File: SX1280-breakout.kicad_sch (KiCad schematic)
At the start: 36 parts, among them J1 Conn_01x01, J10 Conn_01x01, J11 Conn_01x01, J12 Conn_01x01, J13 Conn_01x01, J14 Conn_01x01, J15 Conn_01x01, J16 Conn_01x01, J17 u.FL, J18 u.FL, J2 Conn_01x01, J3 Conn_01x01, J4 Conn_01x01, J5 Conn_01x01, J6 Conn_01x01, J7 Conn_01x01, J8 Conn_01x01, J9 Conn_01x01, U1 SX1280IMLTRT, U2 2450FM07D0034T, U3 EP2W+, X1 52.000 MHz

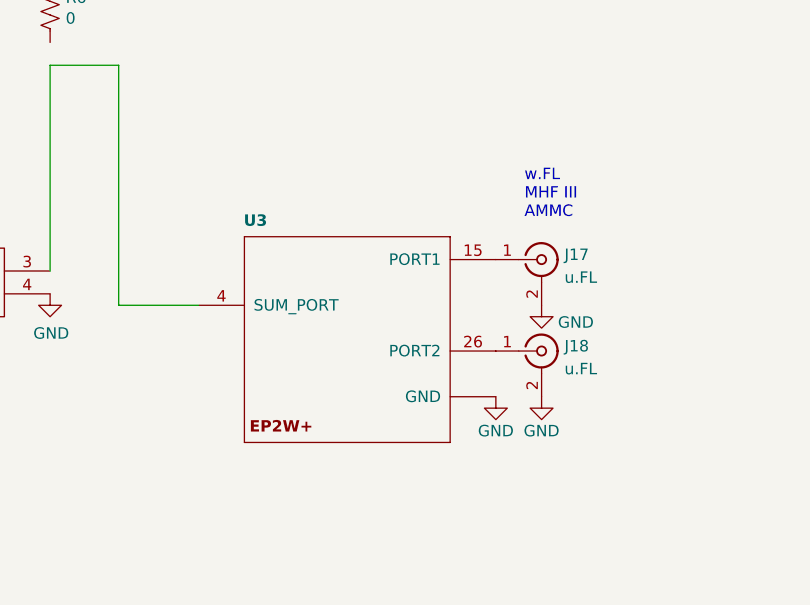
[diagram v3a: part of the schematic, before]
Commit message: back to single antenna
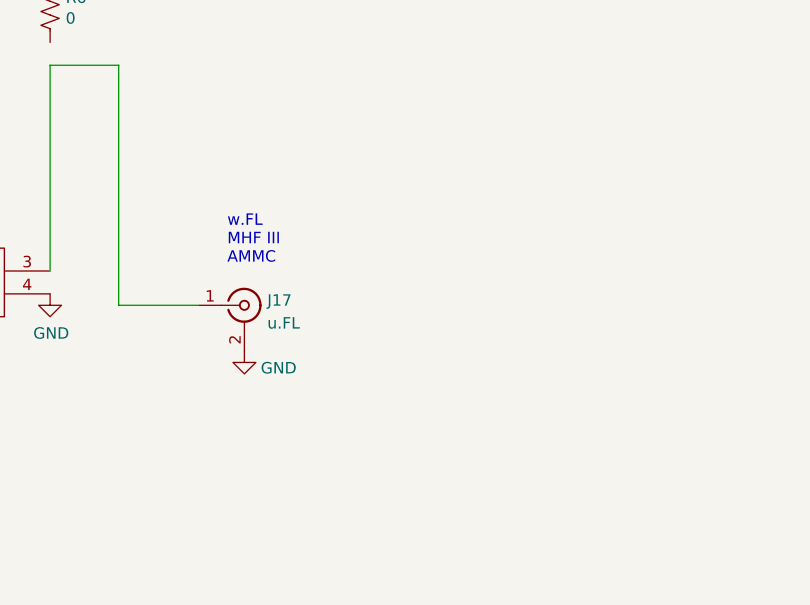
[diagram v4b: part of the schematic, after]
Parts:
- removed J18: u.FL, Connector_Coaxial:U.FL_Hirose_U.FL-R-SMT-1_Vertical, symbol Connector:Conn_Coaxial
- removed U3: EP2W+, custom-footprints:QFN32-5X5MM, symbol mainboard:EP2W+
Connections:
- net at U2.3 (OUT): now also J17.1 (In)
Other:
- moved on the sheet: J17
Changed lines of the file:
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@@
     (effects (font (size 3.9878 3.9878) (thickness 0.7976) bold) (justify left bottom))
   )
-  (text "w.FL\nMHF III\nAMMC" (at 255.905 97.155 0)
+  (text "w.FL\nMHF III\nAMMC" (at 222.885 102.235 0)
     (effects (font (size 1.27 1.27)) (justify left bottom))
   )
@@
     (pin "2")
   )
-  (symbol (lib_id "power:GND") (at 257.81 106.68 0) (unit 1)
-    (in_bom yes) (on_board yes)
-    (property "Reference" "#PWR0107" (id 0) (at 257.81 113.03 0)
-      (effects (font (size 1.27 1.27)) hide)
-    )
-    (property "Value" "GND" (id 1) (at 261.62 108.585 0))
-    (property "Footprint" "" (id 2) (at 257.81 106.68 0)
-      (effects (font (size 1.27 1.27)) hide)
-    )
-    (property "Datasheet" "" (id 3) (at 257.81 106.68 0)
-      (effects (font (size 1.27 1.27)) hide)
-    )
-    (pin "1")
-  )
-  (symbol (lib_id "Connector:Conn_Coaxial") (at 257.81 111.76 0) (unit 1)
+  (symbol (lib_id "power:GND") (at 224.79 111.76 0) (unit 1)
+    (in_bom yes) (on_board yes)
+    (property "Reference" "#PWR0107" (id 0) (at 224.79 118.11 0)
+      (effects (font (size 1.27 1.27)) hide)
+    )
+    (property "Value" "GND" (id 1) (at 228.6 113.665 0))
+    (property "Footprint" "" (id 2) (at 224.79 111.76 0)
+      (effects (font (size 1.27 1.27)) hide)
+    )
+    (property "Datasheet" "" (id 3) (at 224.79 111.76 0)
+      (effects (font (size 1.27 1.27)) hide)
+    )
+    (pin "1")
+  )
+  (symbol (lib_id "Connector:Conn_Coaxial") (at 224.79 106.68 0) (unit 1)
     (in_bom yes) (on_board yes) (fields_autoplaced)
-    (property "Reference" "J18" (id 0) (at 260.3501 111.2185 0)
-      (effects (font (size 1.27 1.27)) (justify left))
-    )
-    (property "Value" "u.FL" (id 1) (at 260.3501 113.7554 0)
-      (effects (font (size 1.27 1.27)) (justify left))
-    )
-    (property "Footprint" "Connector_Coaxial:U.FL_Hirose_U.FL-R-SMT-1_Vertical" (id 2) (at 257.81 111.76 0)
-      (effects (font (size 1.27 1.27)) hide)
-    )
-    (property "Datasheet" " ~" (id 3) (at 257.81 111.76 0)
-      (effects (font (size 1.27 1.27)) hide)
-    )
-    (pin "1")
-    (pin "2")
-  )
-  (symbol (lib_id "power:GND") (at 257.81 116.84 0) (unit 1)
-    (in_bom yes) (on_board yes)
-    (property "Reference" "#PWR0109" (id 0) (at 257.81 123.19 0)
-      (effects (font (size 1.27 1.27)) hide)
-    )
-    (property "Value" "GND" (id 1) (at 257.81 120.65 0))
-    (property "Footprint" "" (id 2) (at 257.81 116.84 0)
-      (effects (font (size 1.27 1.27)) hide)
-    )
-    (property "Datasheet" "" (id 3) (at 257.81 116.84 0)
-      (effects (font (size 1.27 1.27)) hide)
-    )
-    (pin "1")
-  )
-  (symbol (lib_id "Connector:Conn_Coaxial") (at 257.81 101.6 0) (unit 1)
-    (in_bom yes) (on_board yes) (fields_autoplaced)
-    (property "Reference" "J17" (id 0) (at 260.3501 101.0585 0)
-      (effects (font (size 1.27 1.27)) (justify left))
-    )
-    (property "Value" "u.FL" (id 1) (at 260.3501 103.5954 0)
-      (effects (font (size 1.27 1.27)) (justify left))
-    )
-    (property "Footprint" "Connector_Coaxial:U.FL_Hirose_U.FL-R-SMT-1_Vertical" (id 2) (at 257.81 101.6 0)
-      (effects (font (size 1.27 1.27)) hide)
-    )
-    (property "Datasheet" " ~" (id 3) (at 257.81 101.6 0)
-      (effects (font (size 1.27 1.27)) hide)
-    )
-    (pin "1")
-    (pin "2")
-  )
-  (symbol (lib_id "power:GND") (at 252.73 116.84 0) (unit 1)
-    (in_bom yes) (on_board yes)
-    (property "Reference" "#PWR0108" (id 0) (at 252.73 123.19 0)
-      (effects (font (size 1.27 1.27)) hide)
-    )
-    (property "Value" "GND" (id 1) (at 252.73 120.65 0))
-    (property "Footprint" "" (id 2) (at 252.73 116.84 0)
-      (effects (font (size 1.27 1.27)) hide)
-    )
-    (property "Datasheet" "" (id 3) (at 252.73 116.84 0)
-      (effects (font (size 1.27 1.27)) hide)
-    )
-    (pin "1")
-  )
-  (symbol (lib_id "mainboard:EP2W+") (at 237.49 106.68 0) (unit 1)
-    (in_bom yes) (on_board yes)
-    (property "Reference" "U3" (id 0) (at 227.33 96.52 0)
-      (effects (font (size 1.27 1.27) bold) (justify right top))
-    )
-    (property "Value" "EP2W+" (id 1) (at 237.49 106.68 0)
-      (effects (font (size 1.27 1.27)) hide)
-    )
-    (property "Footprint" "custom-footprints:QFN32-5X5MM" (id 2) (at 237.49 106.68 0)
-      (effects (font (size 1.27 1.27)) hide)
-    )
-    (property "Datasheet" "https://www.minicircuits.com/pdfs/EP2W+.pdf" (id 3) (at 237.49 106.68 0)
-      (effects (font (size 1.27 1.27)) hide)
-    )
-    (property "Description" "RF Splitter DC-Pass" (id 5) (at 237.49 106.68 0)
-      (effects (font (size 1.27 1.27)) hide)
-    )
-    (property "Flight" "EP2W+" (id 6) (at 237.49 106.68 0)
-      (effects (font (size 1.27 1.27)) hide)
-    )
-    (property "Manufacturer_Name" "Mini Circuits" (id 7) (at 237.49 106.68 0)
-      (effects (font (size 1.27 1.27)) hide)
-    )
-    (property "Manufacturer_Part_Number" "EP2W+" (id 8) (at 237.49 106.68 0)
-      (effects (font (size 1.27 1.27)) hide)
-    )
-    (pin "1")
-    (pin "10")
-    (pin "11")
-    (pin "12")
-    (pin "13")
-    (pin "14")
-    (pin "15")
-    (pin "16")
-    (pin "17")
-    (pin "18")
-    (pin "19")
-    (pin "2")
-    (pin "20")
-    (pin "21")
-    (pin "22")
-    (pin "23")
-    (pin "24")
-    (pin "25")
-    (pin "26")
-    (pin "27")
-    (pin "28")
-    (pin "29")
-    (pin "3")
-    (pin "30")
-    (pin "31")
-    (pin "32")
-    (pin "4")
-    (pin "5")
-    (pin "6")
-    (pin "7")
-    (pin "8")
-    (pin "9")
-    (pin "EP")
+    (property "Reference" "J17" (id 0) (at 227.3301 106.1385 0)
+      (effects (font (size 1.27 1.27)) (justify left))
+    )
+    (property "Value" "u.FL" (id 1) (at 227.3301 108.6754 0)
+      (effects (font (size 1.27 1.27)) (justify left))
+    )
+    (property "Footprint" "Connector_Coaxial:U.FL_Hirose_U.FL-R-SMT-1_Vertical" (id 2) (at 224.79 106.68 0)
+      (effects (font (size 1.27 1.27)) hide)
+    )
+    (property "Datasheet" " ~" (id 3) (at 224.79 106.68 0)
+      (effects (font (size 1.27 1.27)) hide)
+    )
+    (pin "1")
+    (pin "2")
   )
   (sheet_instances
@@
       (reference "#PWR0107") (unit 1) (value "GND") (footprint "")
     )
-    (path "/8cf544d3-5d2f-402c-bf39-04d87279bdea"
-      (reference "#PWR0108") (unit 1) (value "GND") (footprint "")
-    )
-    (path "/33e15a5b-9c50-478f-bd5b-f828403b32a3"
-      (reference "#PWR0109") (unit 1) (value "GND") (footprint "")
-    )
     (path "/00000000-0000-0000-0000-00005d611e57"
       (reference "C1") (unit 1) (value "100nF") (footprint "Capacitor_SMD:C_0402_1005Metric")
@@
       (reference "J17") (unit 1) (value "u.FL") (footprint "Connector_Coaxial:U.FL_Hirose_U.FL-R-SMT-1_Vertical")
     )
-    (path "/144e921c-09f9-4e46-8904-db378eb2dd88"
-      (reference "J18") (unit 1) (value "u.FL") (footprint "Connector_Coaxial:U.FL_Hirose_U.FL-R-SMT-1_Vertical")
-    )
     (path "/00000000-0000-0000-0000-00005d18add6"
       (reference "L1") (unit 1) (value "15uH") (footprint "Inductor_SMD:L_0805_2012Metric")
@@
       (reference "U2") (unit 1) (value "2450FM07D0034T") (footprint "custom-footprints:2450FM07D0034T")
     )
-    (path "/e88eff66-38b6-4df2-a4c3-c0cb54f3031b"
-      (reference "U3") (unit 1) (value "EP2W+") (footprint "custom-footprints:QFN32-5X5MM")
-    )
     (path "/00000000-0000-0000-0000-00005d18c449"
